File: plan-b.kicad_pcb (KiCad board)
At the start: 4 copper layers, 16 x 42 mm, 68 parts, among them J1 HRO_TYPE-C-31-M-14, J2 Battery, J3 rgb, J4 columns, J5 Conn_01x10, J6 rows, J7 sensor, J8 Conn_ARM_SWD_TagConnect_TC203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, J9 Conn_01x05_Pin, J99 Net tie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

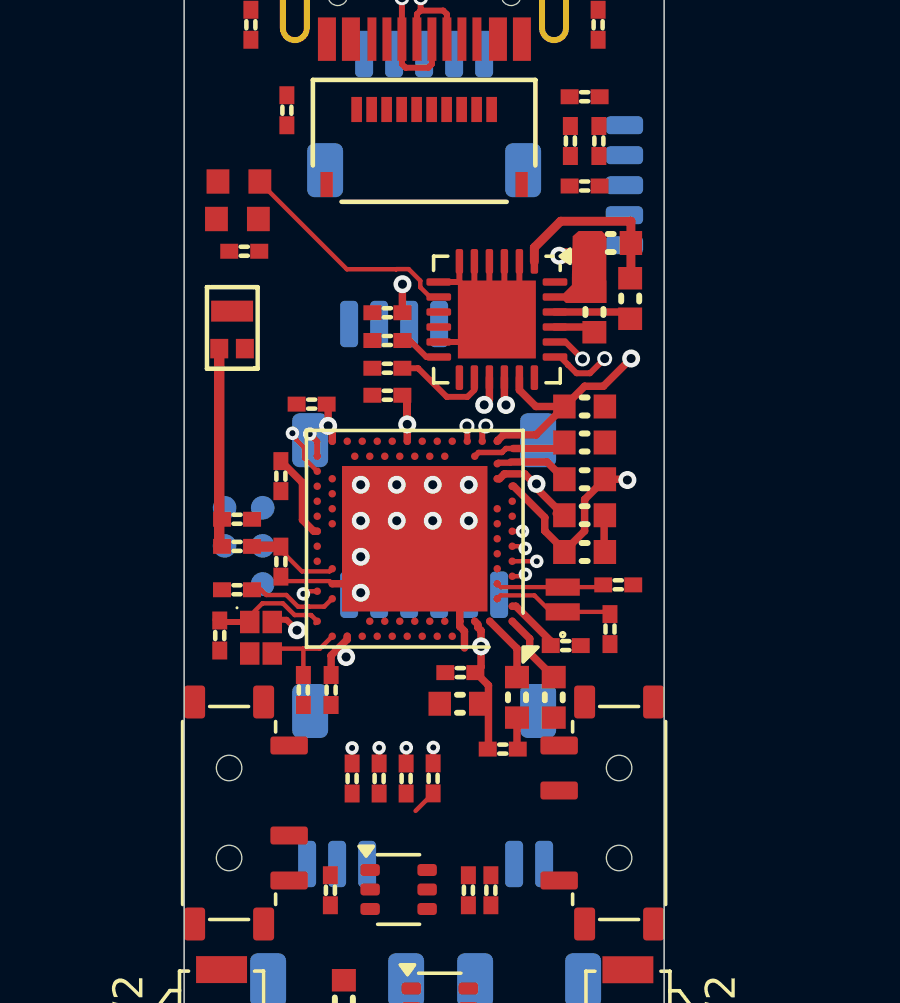
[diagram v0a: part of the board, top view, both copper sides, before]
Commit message: Cleaning up the sensor signals routing
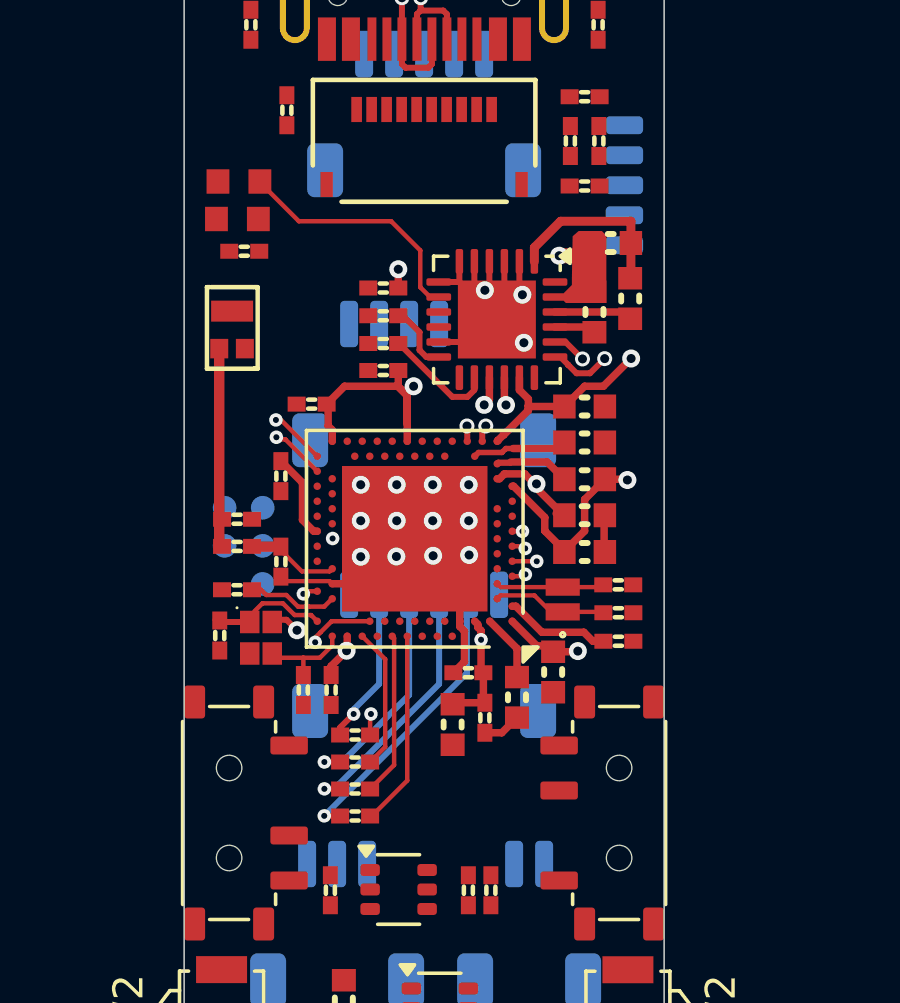
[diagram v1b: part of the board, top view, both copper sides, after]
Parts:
- C19: value 4.7µF -> 10µF
- moved R11 2.89 mm to (147.7, 90.1), turned to 180 degrees
- moved C5 1.76 mm to (156.5, 84.3)
- moved R14 1.74 mm to (147.7, 89.2), turned to 180 degrees
- moved R16 1.45 mm to (147.7, 87.4), turned to 180 degrees
- moved L3 1.20 mm to (152.0, 86.8), turned to -90 degrees
- moved R15 0.97 mm to (147.7, 88.3), turned to 180 degrees
- moved C14 0.85 mm to (154.3, 85.3)
- moved C22 0.84 mm to (148.6, 72.5)
- moved C7 0.84 mm to (148.6, 75.2)
- moved R3 0.84 mm to (148.6, 74.4)
- moved R_ICHG1 0.84 mm to (148.6, 73.4)
- moved C15 0.73 mm to (150.9, 87.0), turned to 90 degrees
- moved C17 0.61 mm to (156.5, 83.3), turned to 0 degrees
- moved C16 0.27 mm to (151.5, 85.3)
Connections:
- net DATA renamed LCD DATA
- U1 pad A14: unconnected-(U1-P1.15-PadA14) -> Sensor CS
- U1 pad A16: unconnected-(U1-P1.13-PadA16) -> Sensor SDIO
- U1 pad A20: unconnected-(U1-P1.10-PadA20) -> Sensor CLK
- U1 pad B19: unconnected-(U1-P1.11-PadB19) -> Sensor IRQ
- U1 pad G1: Sensor CS -> unconnected-(U1-P0.26-PadG1)
- U1 pad J1: Sensor SDIO -> unconnected-(U1-P0.04/AIN2-PadJ1)
- U1 pad L1: Sensor CLK -> unconnected-(U1-P0.06-PadL1)
- U1 pad N1: Sensor IRQ -> unconnected-(U1-P0.08-PadN1)
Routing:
- net Net-(J7-Pin_2): track 0.53 -> 9.90 mm
- net Net-(J7-Pin_3): track 0.53 -> 8.77 mm
- net Net-(J7-Pin_4): track 0.53 -> 7.62 mm
- net Sensor CS: track 1.29 -> 6.54 mm, vias 1 -> 0
- net Net-(J7-Pin_5): track 0.52 -> 5.21 mm
- net VDD: track 14.5 -> 19.2 mm
- net Sensor SDIO: track 0.82 -> 5.46 mm, vias 1 -> 0
- net Sensor CLK: track 0.46 -> 4.72 mm, vias 1 -> 0
- net Sensor IRQ: track 0.34 -> 2.91 mm, vias 1 -> 3
- net Net-(U1-DEC1): track 1.91 -> 3.53 mm
- net GND: track 20.3 -> 19.1 mm, vias 11 -> 16
- net SWDIO: track 0.85 -> 1.88 mm
- net VBUS: track 7.75 -> 6.93 mm
- net unconnected-(U1-P0.04/AIN2-PadJ1): track 0.00 -> 0.82 mm, vias 0 -> 1
- net Net-(U2-ICHG): track 1.44 -> 2.11 mm
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
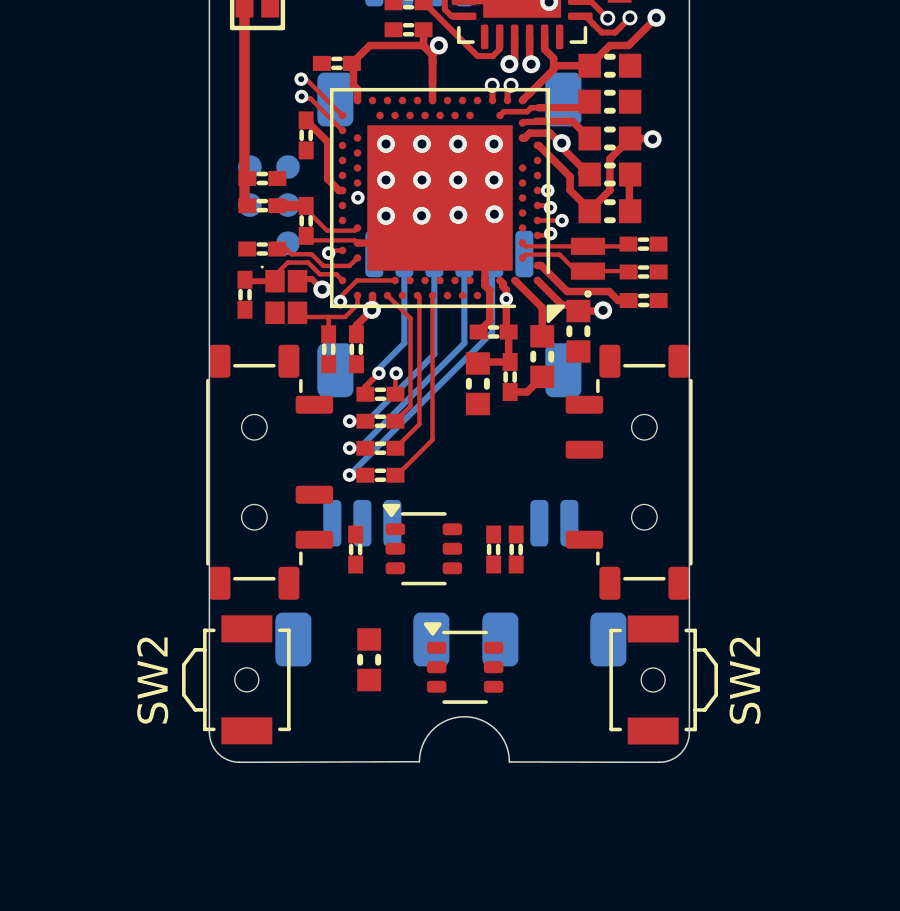
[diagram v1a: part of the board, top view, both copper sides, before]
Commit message: Wiring up the load swiches side of the PCB
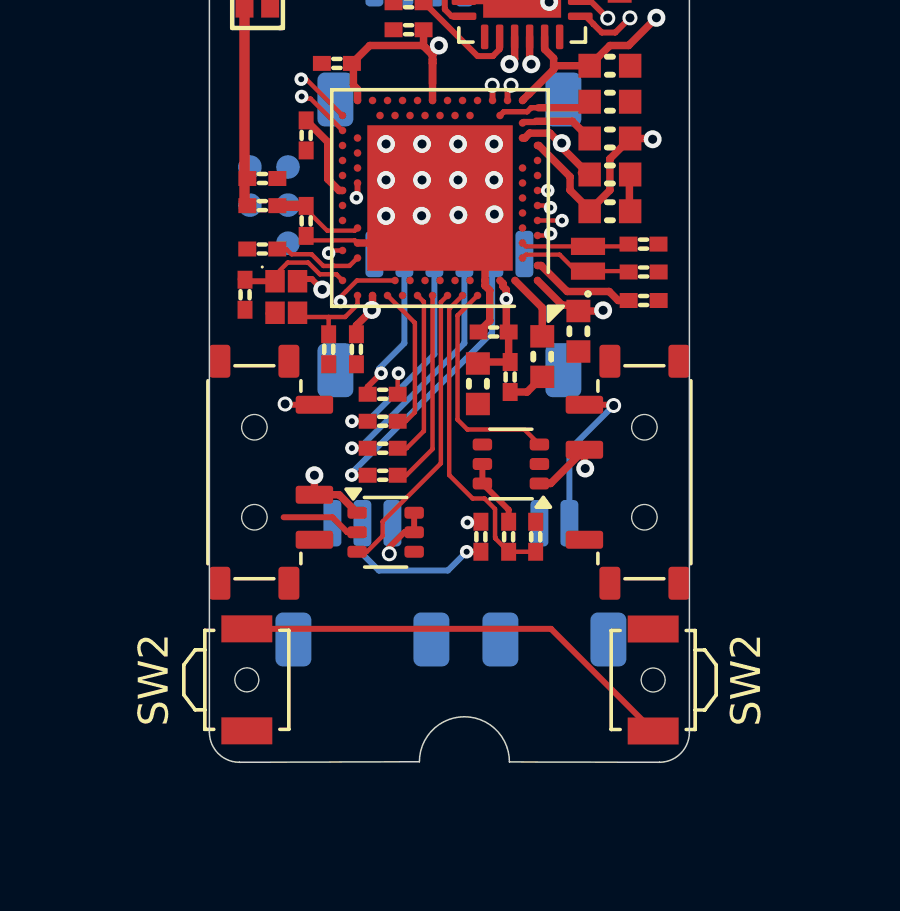
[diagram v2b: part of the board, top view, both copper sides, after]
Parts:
- removed C44: 10µF, Library:C_0603_1608
- moved U4 5.22 mm to (147.9, 92.0)
- moved R8 4.20 mm to (151.1, 92.2)
- moved U3 4.05 mm to (152.1, 89.7), turned to 180 degrees
- moved R_DIV2 1.46 mm to (152.9, 92.1), turned to 90 degrees
- moved R_DIV1 0.49 mm to (152.0, 92.2), turned to -90 degrees
- moved R11 0.08 mm to (147.8, 90.1)
- moved R14 0.08 mm to (147.8, 89.2)
- moved R15 0.08 mm to (147.8, 88.3)
- moved R16 0.08 mm to (147.8, 87.4)
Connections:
- net LCD DATA renamed DATA
- U1 pad A10: unconnected-(U1-P0.29/AIN5-PadA10) -> VSENSE
- U1 pad A12: unconnected-(U1-P0.02/AIN0-PadA12) -> RGB ON
- U1 pad A8: unconnected-(U1-P0.31/AIN7-PadA8) -> VSENSE_ON
- U1 pad P23: unconnected-(U1-P1.07-PadP23) -> RGB DATA
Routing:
- net Net-(J2-Pin_1): track 0.00 -> 17.5 mm, vias 0 -> 2
- net RST: track 0.00 -> 15.0 mm
- net RGB DATA: track 0.00 -> 14.7 mm, vias 0 -> 2
- net VBAT: track 1.60 -> 16.0 mm, vias 2 -> 4
- net VSENSE: track 0.00 -> 10.7 mm
- net RGB ON: track 0.00 -> 9.98 mm
- net VSENSE_ON: track 0.00 -> 7.49 mm
- net Net-(U1-DEC4): track 4.36 -> 10.9 mm
- net Net-(J3-Pin_2): track 0.00 -> 5.46 mm, vias 0 -> 1
- net Sensor IRQ: track 2.91 -> 6.07 mm, vias 3 -> 2
- net Net-(J3-Pin_1): track 0.00 -> 2.96 mm, vias 0 -> 1
- net GND: track 19.1 -> 21.8 mm
- net Net-(U3-QOD): track 0.00 -> 2.29 mm

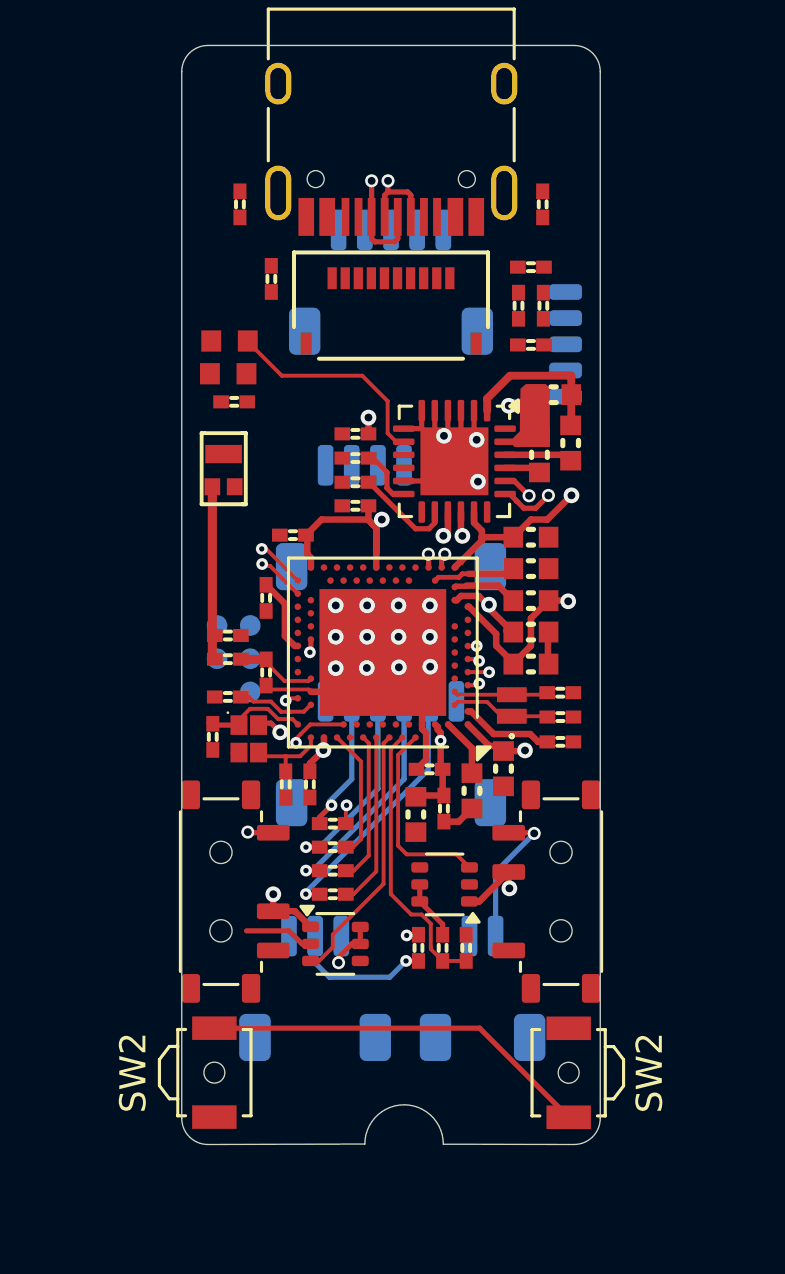
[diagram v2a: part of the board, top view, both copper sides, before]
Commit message: Sorting out most of the powerlines
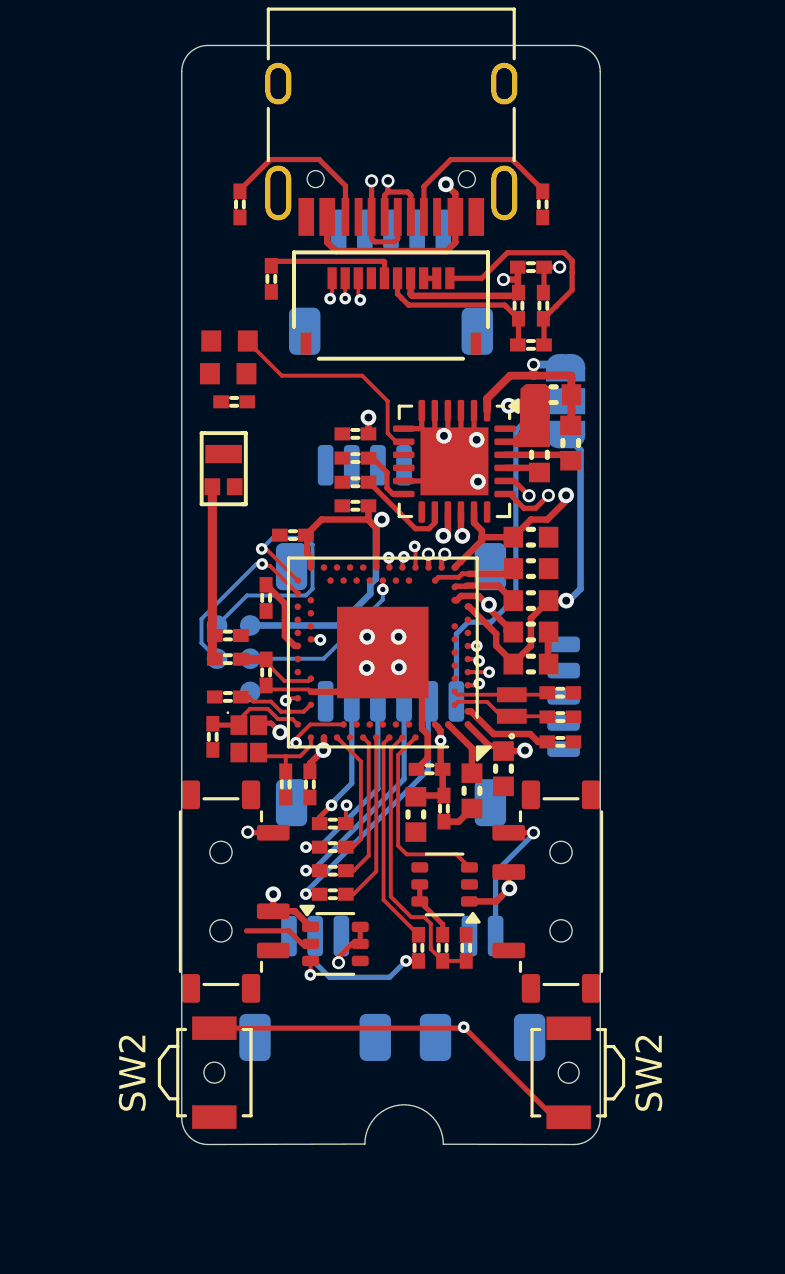
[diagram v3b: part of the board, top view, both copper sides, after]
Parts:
- added JP1: SolderJumper_3_Open, Jumper:SolderJumper-3_P1.3mm_Open_RoundedPad1.0x1.5mm, B.Cu at (156.7, 71.2)
- moved J9 13.5 mm to (158.3, 82.5)
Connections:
- J7 pad 1: /Optical Sensor/VDD -> Net-(J7-Pin_1)
- U1 pad A12: RGB ON -> RGB DATA
- U1 pad AD10: unconnected-(U1-P0.15-PadAD10) -> DATA
- U1 pad AD12: unconnected-(U1-P0.17-PadAD12) -> CLK
- U1 pad AD8: unconnected-(U1-P0.13-PadAD8) -> CS
- U1 pad P23: RGB DATA -> RGB ON
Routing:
- net VDD: track 19.2 -> 92.9 mm, vias 4 -> 5
- net VBAT: track 16.0 -> 41.7 mm
- net RST: track 15.0 -> 39.7 mm, vias 0 -> 2
- net D+: track 5.81 -> 30.4 mm
- net VBUS: track 6.93 -> 29.2 mm, vias 1 -> 2
- net D-: track 5.99 -> 20.6 mm
- net Net-(J7-Pin_1): track 0.00 -> 14.2 mm
- net CLK: track 0.00 -> 12.4 mm, vias 0 -> 2
- net DATA: track 0.00 -> 12.2 mm, vias 0 -> 2
- net CS: track 0.00 -> 12.0 mm, vias 0 -> 2
- net GNDA: track 0.00 -> 8.90 mm
- net SWDIO: track 1.88 -> 10.0 mm
- net Net-(J1-CC1): track 0.00 -> 6.66 mm
- net VDDA: track 0.00 -> 6.63 mm
- net RGB DATA: track 14.7 -> 8.22 mm, vias 2 -> 0
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
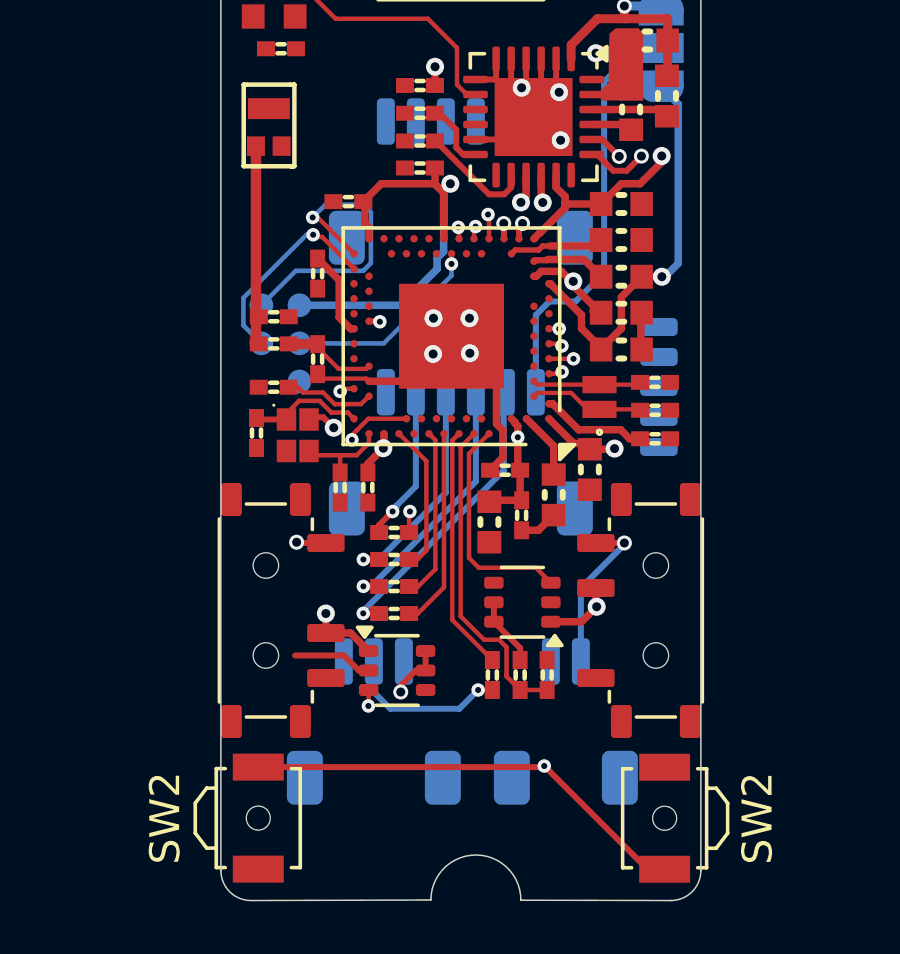
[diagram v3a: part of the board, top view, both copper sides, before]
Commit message: Sorting out other pads and sensor voltage jumper
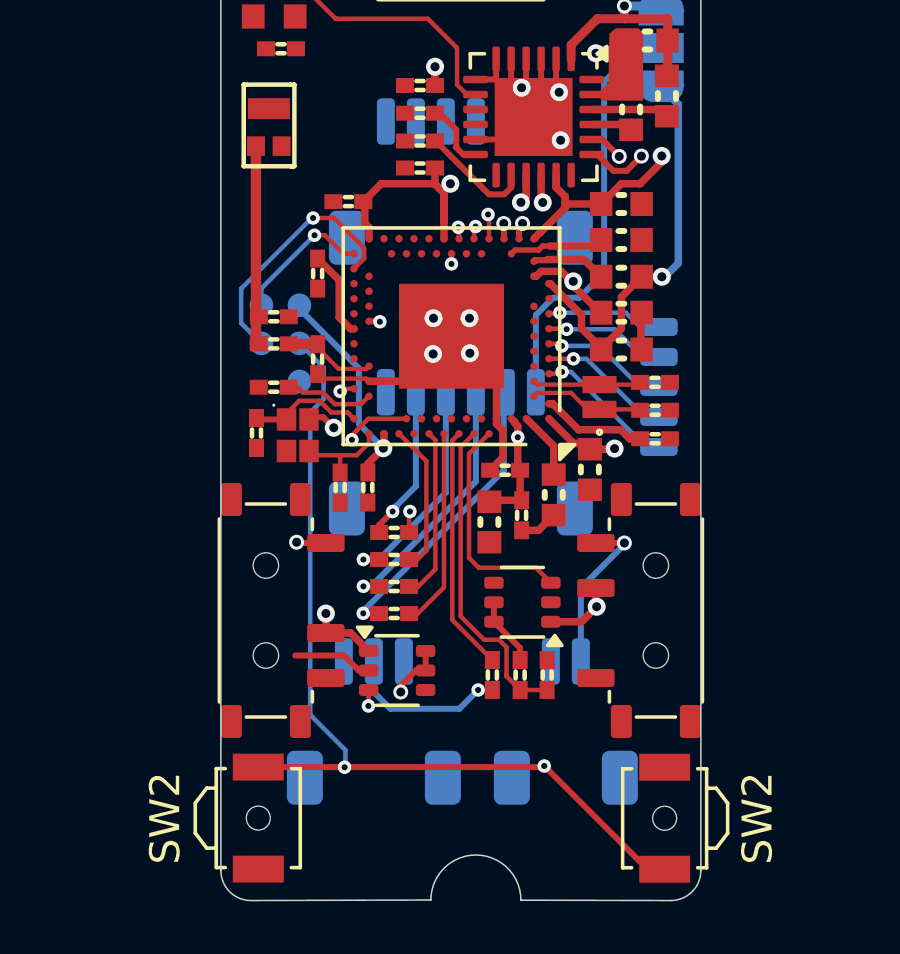
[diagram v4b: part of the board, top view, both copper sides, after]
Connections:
- net DATA renamed LCD DATA
- U1 pad G1: unconnected-(U1-P0.26-PadG1) -> PlanB 5
- U1 pad J1: unconnected-(U1-P0.04/AIN2-PadJ1) -> PlanB 4
- U1 pad L1: unconnected-(U1-P0.06-PadL1) -> PlanB 3
- U1 pad N1: unconnected-(U1-P0.08-PadN1) -> PlanB 2
- U1 pad R1: unconnected-(U1-P1.09-PadR1) -> PlanB 1
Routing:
- net RST: track 39.7 -> 48.5 mm, vias 2 -> 3
- net SWDIO: track 10.0 -> 4.64 mm
- net PlanB 5: track 0.00 -> 4.73 mm, vias 0 -> 1
- net PlanB 4: track 0.00 -> 4.47 mm, vias 0 -> 1
- net PlanB 3: track 0.00 -> 4.26 mm, vias 0 -> 1
- net PlanB 2: track 0.00 -> 4.05 mm, vias 0 -> 1
- net PlanB 1: track 0.00 -> 3.87 mm, vias 0 -> 1
- net VDD: track 92.9 -> 90.9 mm
- net SWCLK: track 6.79 -> 8.42 mm
- net unconnected-(U1-P0.04/AIN2-PadJ1): track 0.82 -> 0.00 mm, vias 1 -> 0
- net unconnected-(U1-P0.26-PadG1): track 0.46 -> 0.00 mm, vias 1 -> 0
- net unconnected-(U1-P0.06-PadL1): track 0.46 -> 0.00 mm, vias 1 -> 0
- net unconnected-(U1-P0.08-PadN1): track 0.34 -> 0.00 mm, vias 1 -> 0
